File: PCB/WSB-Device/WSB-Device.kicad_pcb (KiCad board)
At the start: 4 copper layers, 54 x 29 mm, 86 parts, among them J1 Conn_02x04_Counter_Clockwise, J2 Conn_01x08, J3 USB_C_Receptacle_USB2.0_14P, J4 Conn_01x02, SW1 SW_SPST_4_PIN, SW2 SW_SPST_4_PIN, U1 ESP32-C6FH4, U2 XC6194A303ER-G, U3 USBLC6-2P6, U4 MCP73830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

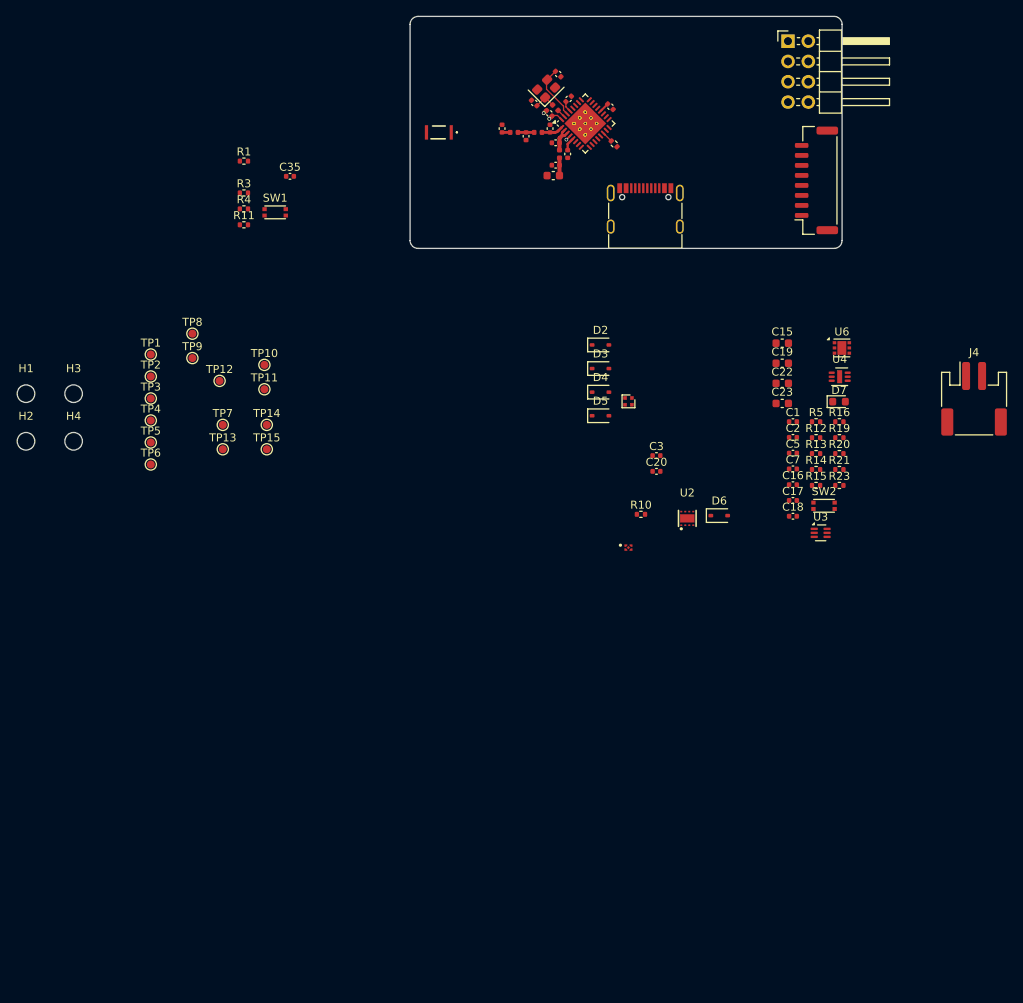
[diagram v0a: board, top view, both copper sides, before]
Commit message: -Corrected test point numbering
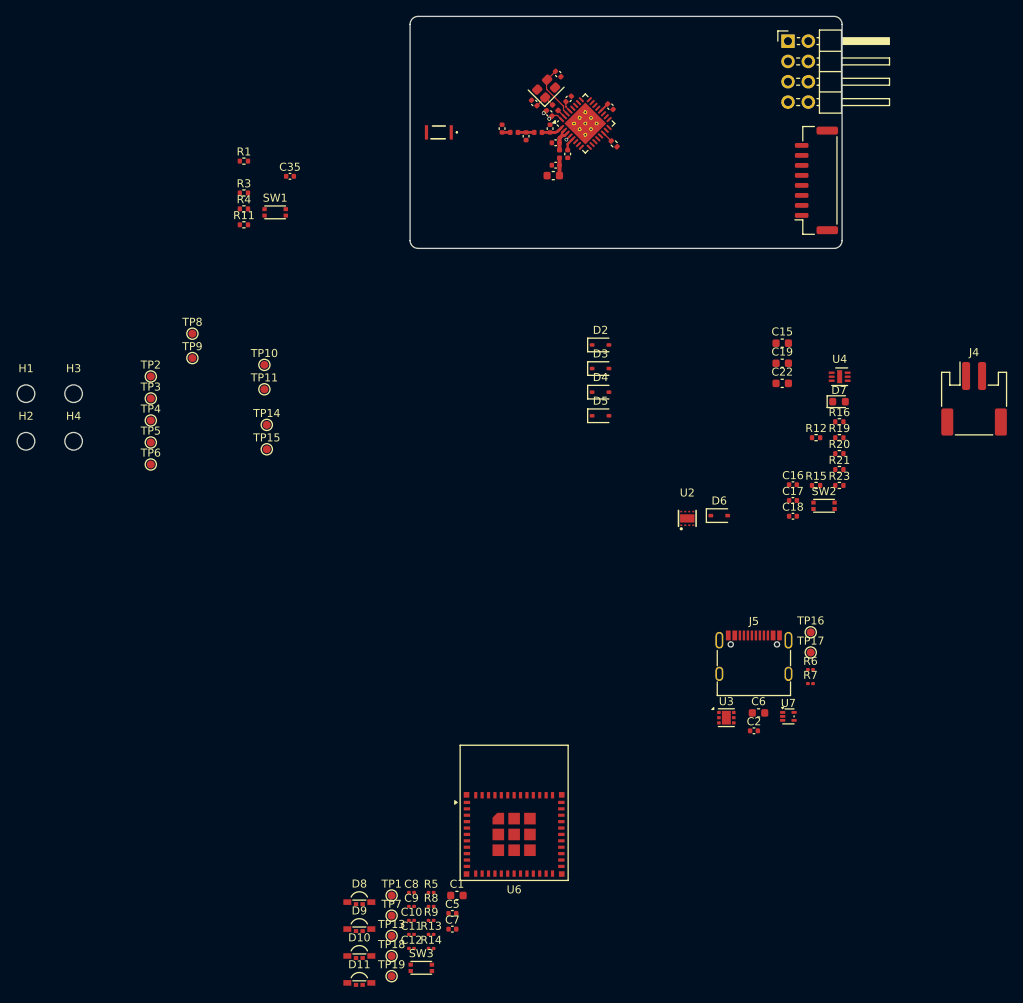
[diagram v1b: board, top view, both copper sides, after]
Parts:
- removed C20, C3: 100nF, Capacitor_SMD:C_0402_1005Metric
- removed C23: 10uF, Capacitor_SMD:C_0603_1608Metric
- removed D1: WS2812B, EN_Designs-Footprints:XL-1010RGBC-WS2812B
- removed J3: USB_C_Receptacle_USB2.0_14P, Connector_USB:USB_C_Receptacle_G-Switch_GT-USB-7010ASV
- removed R10: 470, Resistor_SMD:R_0402_1005Metric
- removed TP12: TestPoint, TestPoint:TestPoint_Pad_D1.0mm
- removed U5: 74LV1T34, EN_Designs-Footprints:X2SON5_0.8x0.8mm_SOT1226
- added C10: 100nF, Capacitor_SMD:C_0201_0603Metric, F.Cu at (82.2, 195.0)
- added C11: 100nF, Capacitor_SMD:C_0201_0603Metric, F.Cu at (82.2, 196.8)
- added C12: 100nF, Capacitor_SMD:C_0201_0603Metric, F.Cu at (82.2, 198.5)
- added C6: 10uF, Capacitor_SMD:C_0603_1608Metric, F.Cu at (125.6, 169.1)
- added C8: 100nF, Capacitor_SMD:C_0201_0603Metric, F.Cu at (82.2, 191.5)
- added C9: 100nF, Capacitor_SMD:C_0201_0603Metric, F.Cu at (82.2, 193.3)
- added D10: ~, EN_Designs-Footprints:XL-3210RGBC-2812B, F.Cu at (75.7, 199.6)
- added D11: ~, EN_Designs-Footprints:XL-3210RGBC-2812B, F.Cu at (75.7, 202.9)
- added D8: ~, EN_Designs-Footprints:XL-3210RGBC-2812B, F.Cu at (75.7, 192.8)
- added D9: ~, EN_Designs-Footprints:XL-3210RGBC-2812B, F.Cu at (75.7, 196.2)
- added J5: USB_C_Receptacle_USB2.0_14P, Connector_USB:USB_C_Receptacle_G-Switch_GT-USB-7010ASV, F.Cu at (125.0, 163.1)
- added R6: 5.1k, Resistor_SMD:R_0201_0603Metric, F.Cu at (132.0, 163.6)
- added R7: 5.1k, Resistor_SMD:R_0201_0603Metric, F.Cu at (132.0, 165.4)
- added R8: 22, Resistor_SMD:R_0201_0603Metric, F.Cu at (84.6, 193.3)
- added R9: 22, Resistor_SMD:R_0201_0603Metric, F.Cu at (84.6, 195.0)
- added SW3: SW_SPST_4_PIN, EN_Designs-Footprints:1TS026A-2300-0553-CT, F.Cu at (83.4, 200.9)
- added TP16: TestPoint, EN_Designs-Footprints:TestPoint_Pad_D1.0mm, F.Cu at (132.1, 159.0)
- added TP17: TestPoint, EN_Designs-Footprints:TestPoint_Pad_D1.0mm, F.Cu at (132.1, 161.5)
- added TP18: TestPoint, EN_Designs-Footprints:TestPoint_Pad_D1.0mm, F.Cu at (79.7, 199.4)
- added TP19: TestPoint, EN_Designs-Footprints:TestPoint_Pad_D1.0mm, F.Cu at (79.7, 202.0)
- added U7: TPD2E2U06DRL, Package_TO_SOT_SMD:SOT-553, F.Cu at (129.3, 169.5)
- C1: value 1uF -> 22uF; footprint Capacitor_SMD:C_0402_1005Metric -> Capacitor_SMD:C_0603_1608Metric
- C2, C5, C7: value 100nF -> 1uF
- R13: value 5.1k -> 10k; footprint Resistor_SMD:R_0402_1005Metric -> Resistor_SMD:R_0201_0603Metric
- R14: value 5.1k -> 470; footprint Resistor_SMD:R_0402_1005Metric -> Resistor_SMD:R_0201_0603Metric
- R5: footprint Resistor_SMD:R_0402_1005Metric -> Resistor_SMD:R_0201_0603Metric
- TP1, TP13, TP7: footprint TestPoint:TestPoint_Pad_D1.0mm -> EN_Designs-Footprints:TestPoint_Pad_D1.0mm
- U3: value USBLC6-2P6 -> NCP187; footprint EN_Designs-Footprints:ST_SOT-666 -> EN_Designs-Footprints:OnSemi_WDFN6_2x2_0.65P_CASE_511BR
- U6: value NCP187 -> ESP32-C6-MINI-1; footprint EN_Designs-Footprints:OnSemi_WDFN6_2x2_0.65P_CASE_511BR -> RF_Module:ESP32-C6-MINI-1
- moved R13 77.0 mm to (84.6, 196.8)
- moved R14 76.8 mm to (84.6, 198.5)
- moved R5 76.0 mm to (84.6, 191.5)
- moved TP1 74.0 mm to (79.7, 191.9)
- moved U6 73.3 mm to (95.0, 184.3)
- moved C1 72.6 mm to (87.9, 191.9)
- moved C5 71.6 mm to (87.3, 194.1)
- moved C7 71.6 mm to (87.3, 196.1)
- moved TP7 64.9 mm to (79.7, 194.4)
- moved TP13 64.4 mm to (79.7, 196.9)
- moved C2 37.0 mm to (125.0, 171.3)
- moved U3 25.9 mm to (121.5, 169.7)
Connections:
- C1 pad 2: Net-(U2-VOUT) -> +3V3
- C2 pad 2: /Power/D- -> Net-(U2-VOUT)
- C5 pad 1: +5V -> GND
- C5 pad 2: GND -> +3V3
- C7 pad 2: /Power/D+ -> /MCU/EN
- R13 pad 1: GND -> /MCU/GPIO9
- R13 pad 2: Net-(J3-CC1) -> +3V3
- R14 pad 1: GND -> Net-(D8-DIN)
- R3 pad 1: /Power/D- -> /MCU/D-
- R4 pad 1: /Power/D+ -> /MCU/D+
- R5 pad 1: /Power/PG -> /MCU/EN
- R5 pad 2: Net-(U2-VOUT) -> +3V3
- TP1 pad 1: +5V -> /MCU/ESP_U0_TX
- TP13 pad 1: GND -> /MCU/EN
- TP7 pad 1: +3V3 -> /MCU/ESP_U0_RX
- U3 pad 1: /Power/D- -> Net-(U2-VOUT)
- U3 pad 2: GND -> Net-(U2-VOUT)
- U3 pad 3: /Power/D+ -> GND
- U3 pad 4: /Power/D+ -> GND
- U3 pad 5: +5V -> +3V3
- U3 pad 6: /Power/D- -> +3V3
- U6 pad 1: Net-(U2-VOUT) -> GND
- U6 pad 2: /Power/PG -> GND
- U6 pad 3: GND -> +3V3
- U6 pad 4: GND -> unconnected-(U6-NC-Pad4)
- U6 pad 5: +3V3 -> unconnected-(U6-IO2-Pad5)
- U6 pad 6: +3V3 -> /MCU/GPIO3
- U6 pad 7: GND -> unconnected-(U6-NC-Pad7)
